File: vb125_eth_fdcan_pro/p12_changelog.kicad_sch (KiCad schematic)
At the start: 0 parts

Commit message: Finish schematics.
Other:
- note added: "* Initial revision based on vg095 design"
- note added: "Rev.A / 21Apr2023"
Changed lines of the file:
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@@
 (kicad_sch (version 20230121) (generator eeschema)
   (paper "A4")
+  (text "* Initial revision based on vg095 design" (at 17.78 25.4 0)
+    (effects (font (size 1.905 1.905)) (justify left bottom))
+  )
+  (text "Rev.A / 21Apr2023" (at 17.78 20.32 0)
+    (effects (font (size 2.54 2.54)) (justify left bottom))
+  )
 )

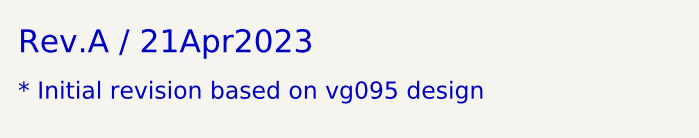
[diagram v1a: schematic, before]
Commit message: Add testpoints and set page templates.
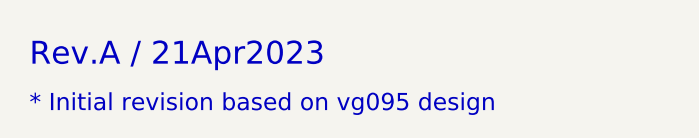
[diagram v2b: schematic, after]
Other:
- company: (none) -> vhrd.tech AS
- title: (none) -> rt_bridge_pro
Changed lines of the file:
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@@
 (kicad_sch (version 20230121) (generator eeschema)
-  (paper "A4")
-  (text "* Initial revision based on vg095 design" (at 17.78 25.4 0)
+  (paper "A3")
+  (title_block
+    (title "rt_bridge_pro")
+    (date "2023-04-21")
+    (rev "A")
+    (company "vhrd.tech AS")
+    (comment 1 "Isaikin R.E.")
+    (comment 4 "Draft")
+  )
+  (text "* Initial revision based on vg095 design" (at 19.05 26.67 0)
     (effects (font (size 1.905 1.905)) (justify left bottom))
   )
-  (text "Rev.A / 21Apr2023" (at 17.78 20.32 0)
+  (text "Rev.A / 21Apr2023" (at 19.05 21.59 0)
     (effects (font (size 2.54 2.54)) (justify left bottom))
   )
